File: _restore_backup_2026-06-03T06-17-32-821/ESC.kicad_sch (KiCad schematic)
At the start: 37 parts, among them Q1 SP40N03GNJ, Q11 SP40N03GNJ, Q3 SP40N03GNJ, Q5 SP40N03GNJ, Q7 SP40N03GNJ, Q9 SP40N03GNJ, U1 AT32F421G8U7, U3 NSG2065Q_C53463328

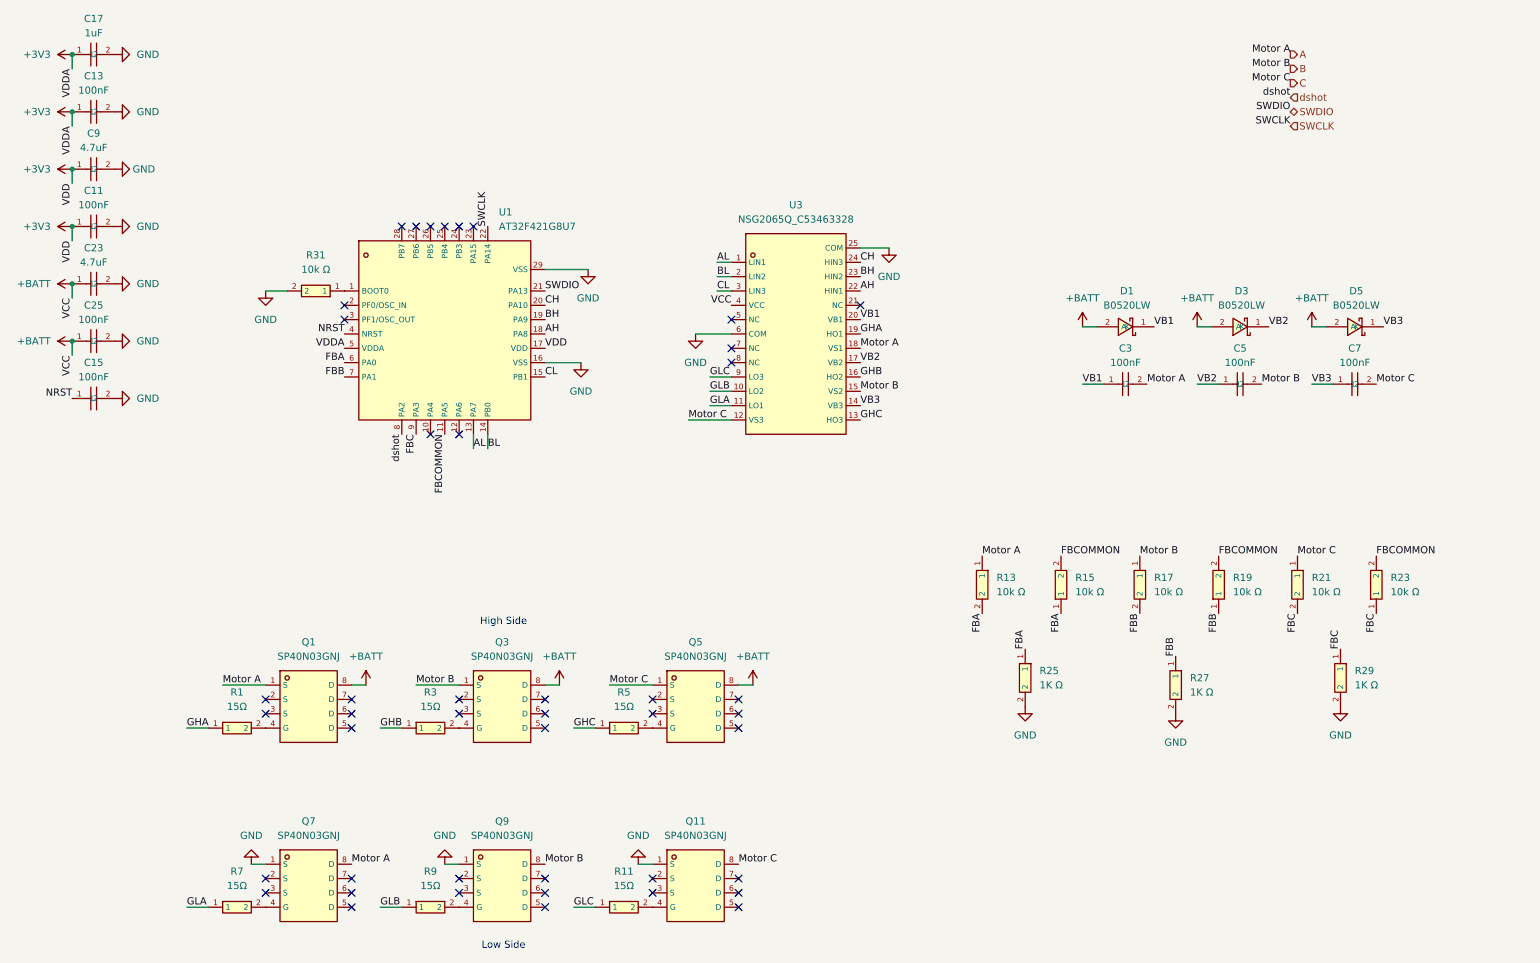
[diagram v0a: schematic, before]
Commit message: Schematic - Completed, PCB - Net Classes Assigned
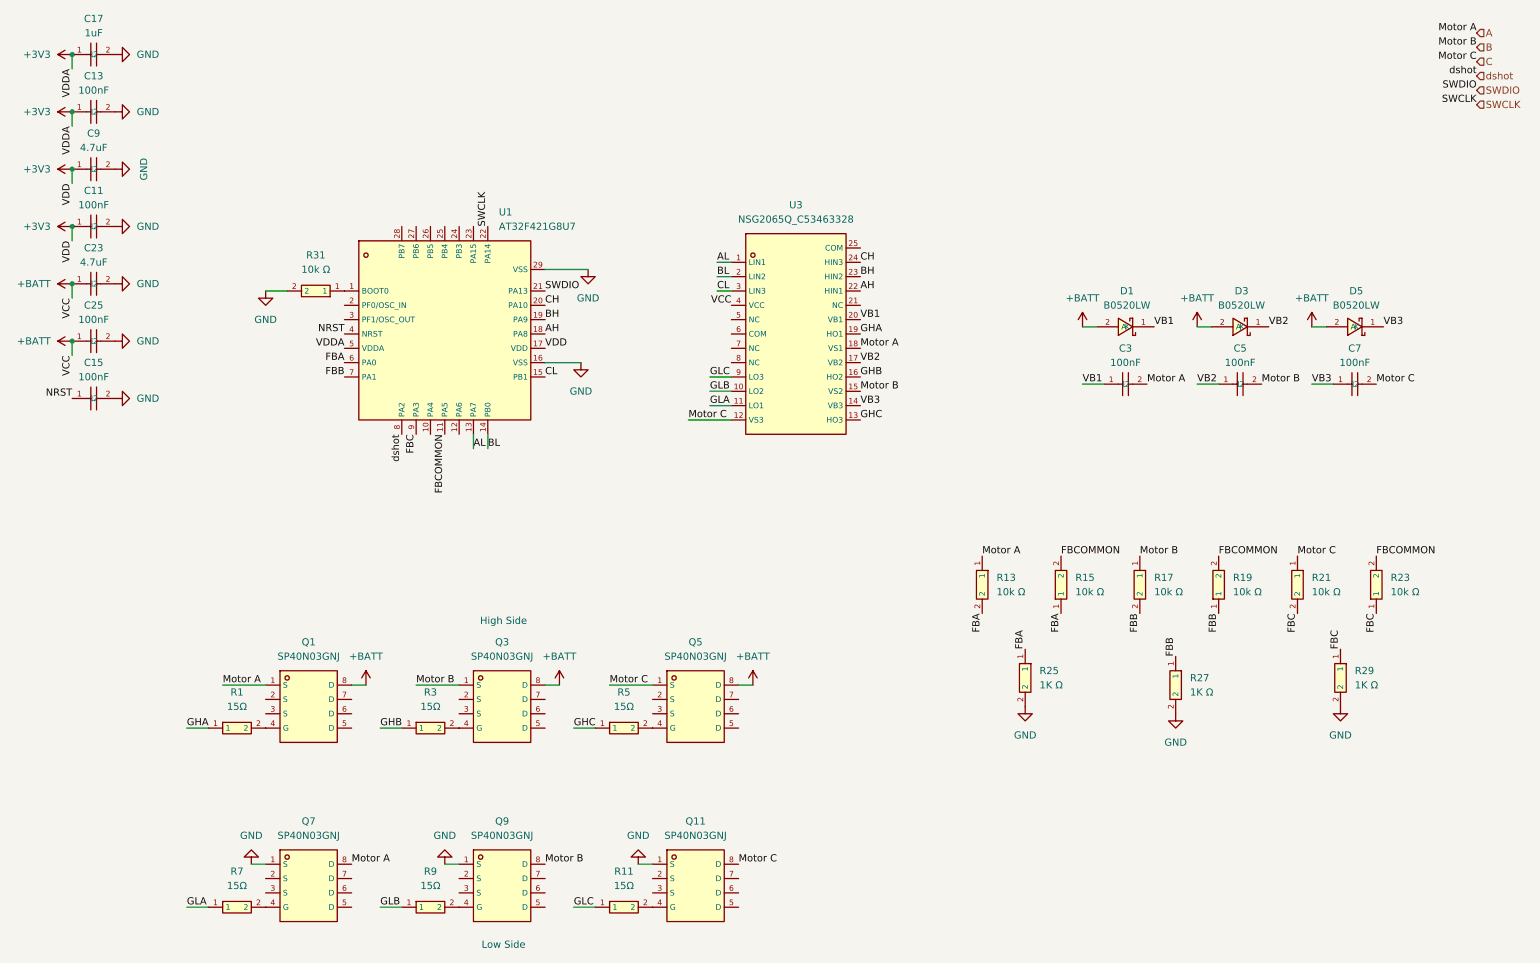
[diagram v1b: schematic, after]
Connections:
- net GND: no longer U3.25 (COM), U3.6 (COM)
- no-connect marks 44 -> 0
